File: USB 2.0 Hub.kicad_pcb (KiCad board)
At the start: 2 copper layers, 57.4 x 27.9 mm, 32 parts, among them J1 USB_C_Receptacle_USB2.0, J2 USB_C_Receptacle_USB2.0, J3 USB_C_Receptacle_USB2.0, J4 USB_C_Receptacle_USB2.0, J5 USB_C_Receptacle_USB2.0, U1 SL2.1A

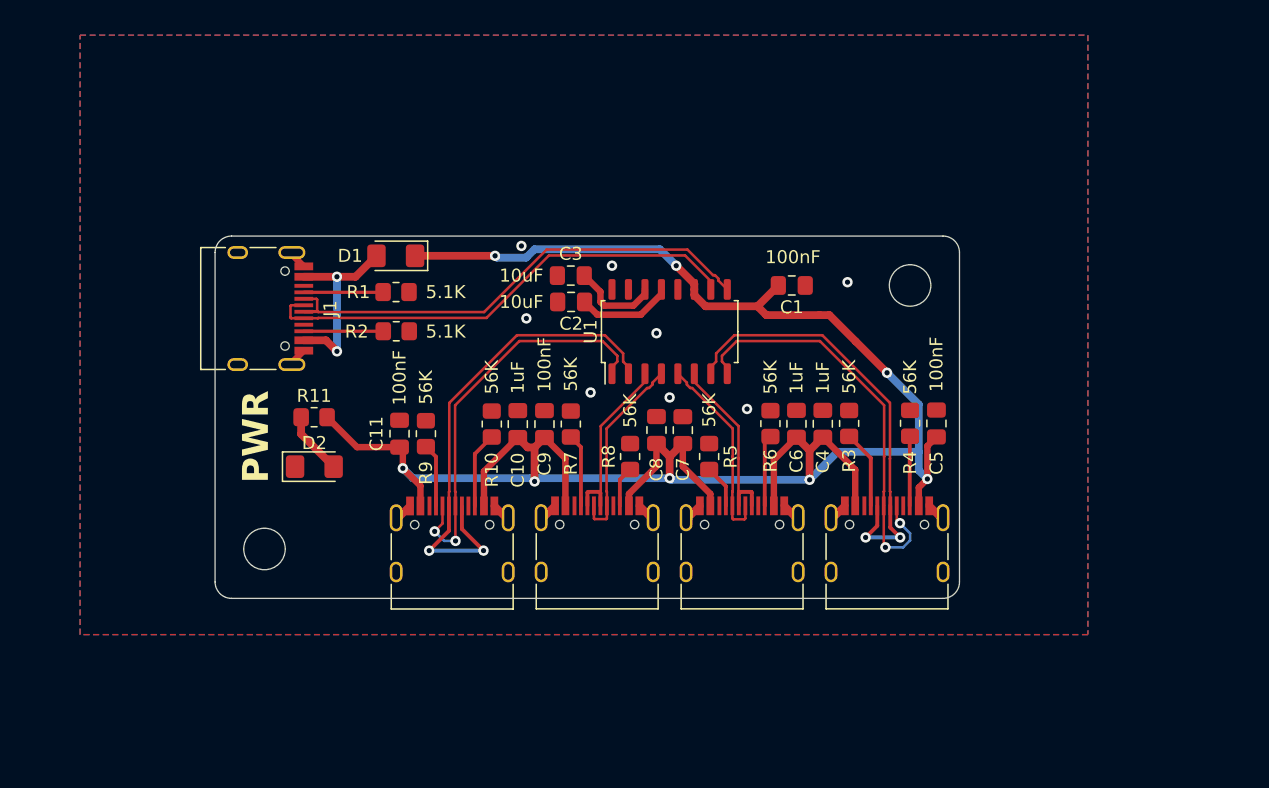
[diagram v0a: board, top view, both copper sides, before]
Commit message: Adjusting size to match wellplate
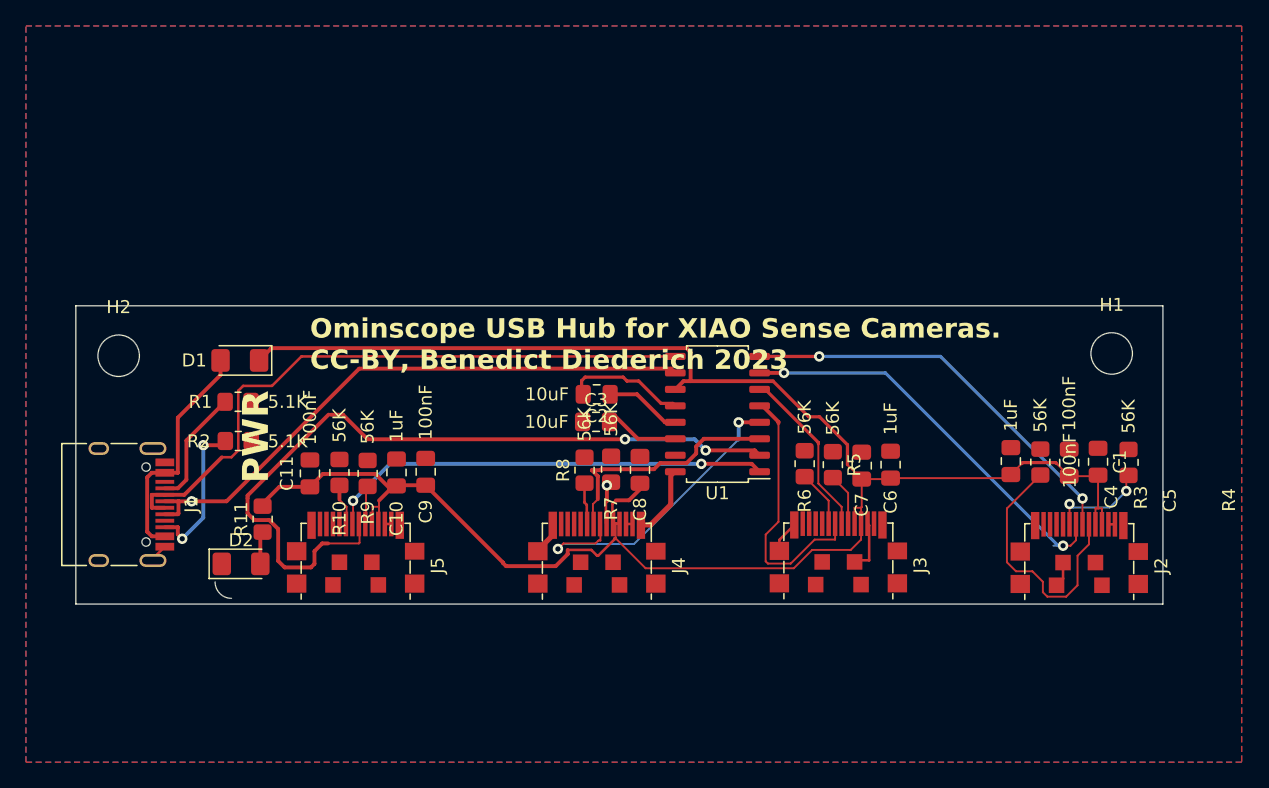
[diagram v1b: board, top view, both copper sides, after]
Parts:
- removed REF** (x2): MountingHole_3.2mm_M3, MountingHole:MountingHole_3.2mm_M3
- added H1: MountingHole, MountingHole:MountingHole_3.2mm_M3_ISO14580, F.Cu at (122.2, 89.8)
- added H2: MountingHole, MountingHole:MountingHole_3.2mm_M3_ISO14580, F.Cu at (45.6, 90.0)
- J2, J3, J4, J5: footprint Connector_USB:USB_C_Receptacle_HRO_TYPE-C-31-M-12 -> uc32_standalone_singlemotor:USB_C_Plug_UTC009-C12
- moved C1 27.2 mm to (121.2, 98.2), turned to -90 degrees
- moved J1 18.5 mm to (45.2, 101.5)
- moved R4 17.1 mm to (123.5, 98.2)
- moved R3 15.0 mm to (116.7, 98.2)
- moved J2 15.0 mm to (119.7, 103.2)
- moved R1 14.8 mm to (54.9, 93.6)
- moved R2 14.8 mm to (54.9, 96.6)
- moved C4 14.8 mm to (114.5, 98.1)
- moved D1 14.5 mm to (55.0, 90.4)
- moved C7 14.1 mm to (103.0, 98.5)
- moved R10 12.3 mm to (62.7, 99.0)
- moved C3 11.4 mm to (82.5, 95.1)
- moved C5 10.7 mm to (119.0, 98.2)
- moved C10 10.1 mm to (67.1, 99.0)
- moved C9 9.87 mm to (69.3, 99.0)
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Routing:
- net /D4+: track 38.2 -> 59.4 mm
- net GND: track 14.5 -> 28.9 mm, vias 8 -> 0
- net Net-(J2-CC1): track 6.05 -> 20.2 mm
- net /VBUS: track 162.8 -> 150.6 mm, vias 8 -> 0
- net /D-: track 39.0 -> 49.5 mm
- net /D3+: track 15.0 -> 25.2 mm, vias 0 -> 2
- net /D+: track 37.8 -> 45.8 mm, vias 0 -> 1
- net Net-(J1-CC2): track 6.13 -> 11.8 mm, vias 0 -> 2
- net /D2-: track 15.0 -> 20.6 mm
- net /D3-: track 14.7 -> 18.7 mm
- net /D4-: track 31.2 -> 34.5 mm
- net Net-(D1-A): track 14.9 -> 18.2 mm, vias 2 -> 0
- net Net-(J1-CC1): track 6.12 -> 9.19 mm
- net Net-(J5-CC2): track 5.86 -> 3.10 mm
- net Net-(J2-CC2): track 5.38 -> 7.86 mm, vias 0 -> 2
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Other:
- board size 57.4 x 27.9 mm -> 83.8 x 23 mm
- board text added: "Ominscope USB Hub for XIAO Sense Cameras. CC-BY, Benedict Diederich 2023"

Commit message: Fixed pending connections
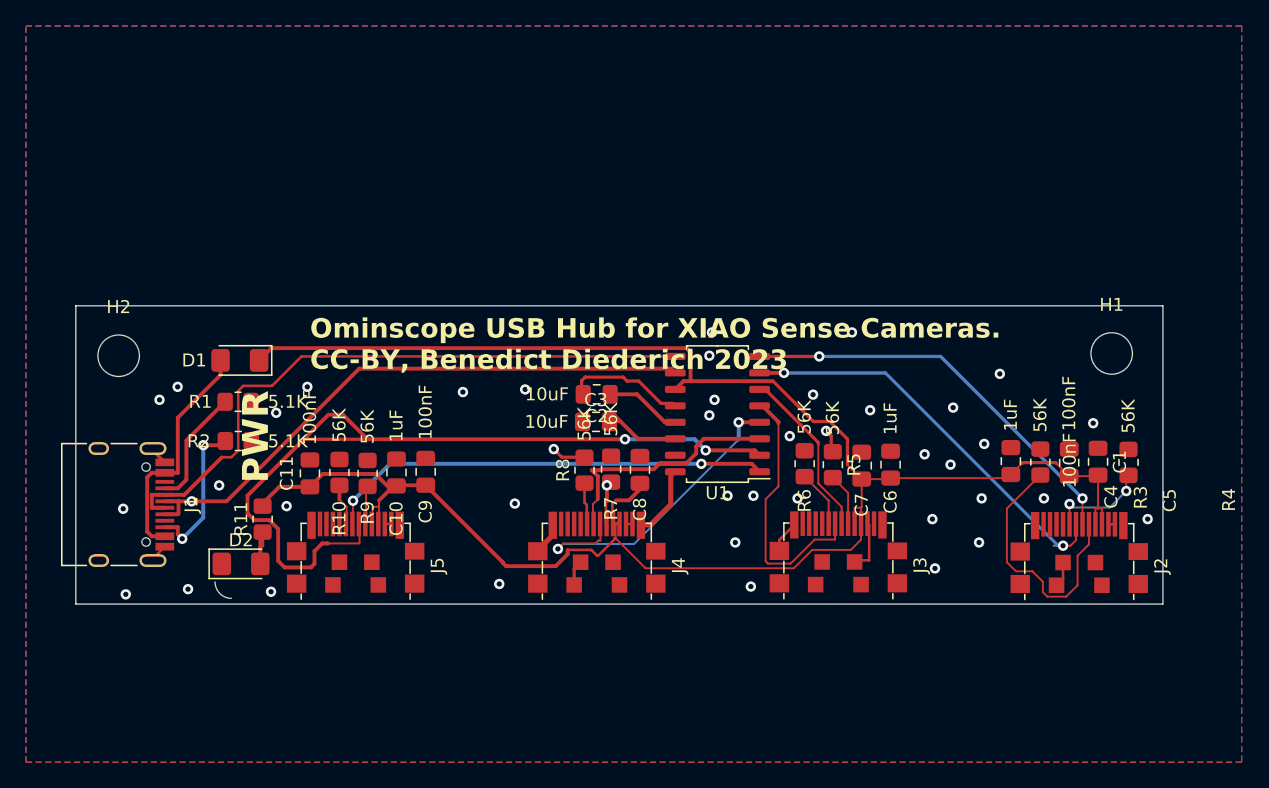
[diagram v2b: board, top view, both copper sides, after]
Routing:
- net GND: track 28.9 -> 36.9 mm, vias 0 -> 41
- net /D4+: track 59.4 -> 64.2 mm
- net Net-(D2-A): track 2.47 -> 3.76 mm
- net Net-(U1-VDD18): track 5.84 -> 6.70 mm

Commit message: Swapping USB connectors
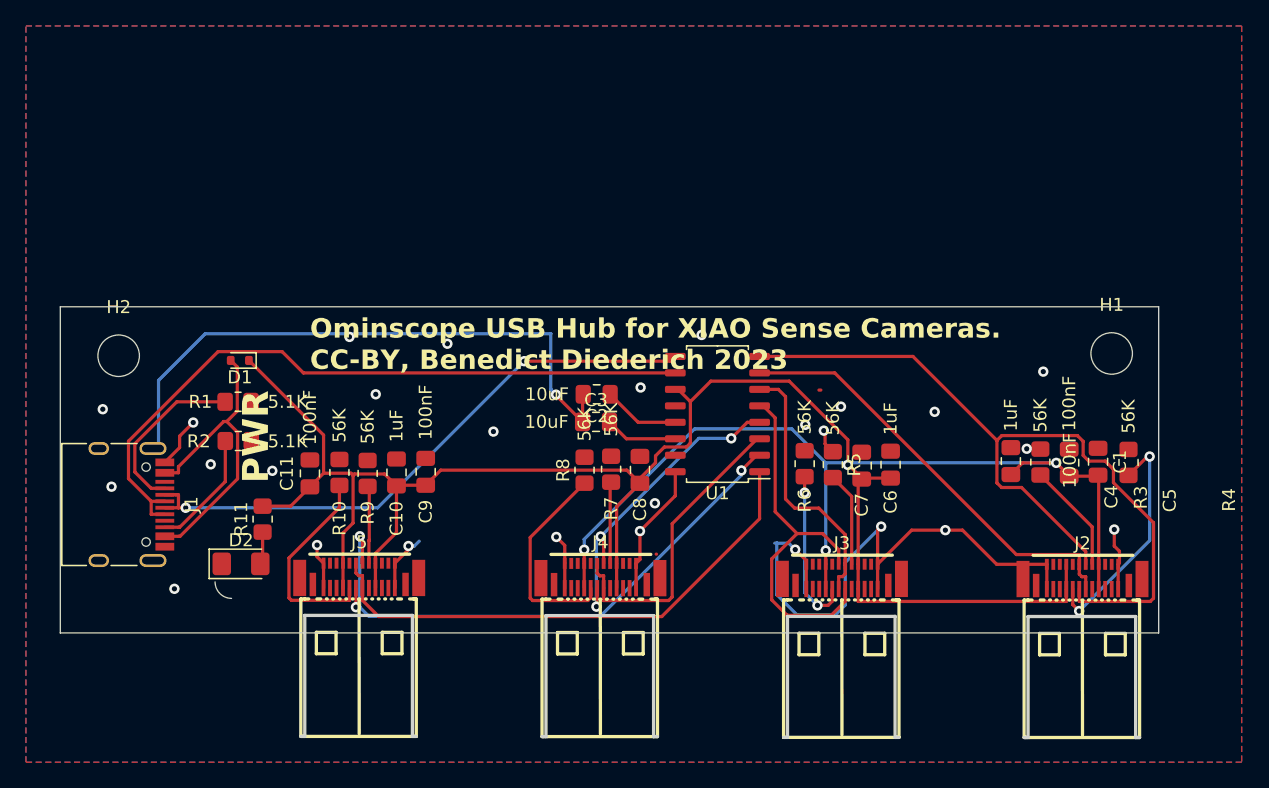
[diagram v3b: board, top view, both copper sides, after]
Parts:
- D1: value SD1206T020S1R0 -> RB521S30T1G; footprint Diode_SMD:D_1206_3216Metric_Pad1.42x1.75mm_HandSolder -> Diode_SMD:D_SOD-523
- J2, J3, J4, J5: footprint uc32_standalone_singlemotor:USB_C_Plug_UTC009-C12 -> Connector_USB:USB_C_Receptacle_U261-241N-4BS2SS
- moved J3 6.96 mm to (101.4, 110.1)
- moved J2 6.91 mm to (120.0, 110.1)
- moved J4 6.87 mm to (82.8, 110.0)
- moved J5 6.86 mm to (64.2, 110.0)
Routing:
- net GND: track 36.9 -> 125.1 mm, vias 41 -> 28
- net /VBUS: track 151.0 -> 199.2 mm, vias 0 -> 4
- net /D1+: track 31.4 -> 63.1 mm, vias 2 -> 0
- net /D4+: track 64.2 -> 45.9 mm, vias 2 -> 3
- net Net-(J4-CC2): track 3.20 -> 16.2 mm
- net Net-(J5-CC2): track 3.10 -> 16.0 mm
- net Net-(J2-CC1): track 20.2 -> 8.54 mm
- net Net-(J2-CC2): track 7.86 -> 18.3 mm
- net /D2-: track 20.6 -> 29.5 mm
- net /D+: track 45.8 -> 54.2 mm, vias 1 -> 0
- net Net-(J3-CC2): track 4.39 -> 12.6 mm, vias 0 -> 2
- net /D2+: track 13.2 -> 20.4 mm
- net /D4-: track 34.5 -> 41.1 mm, vias 2 -> 0
- net Net-(D1-A): track 18.2 -> 24.2 mm
- net /D3-: track 18.7 -> 23.7 mm
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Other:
- board size 83.8 x 23 mm -> 84.7 x 25.2 mm

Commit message: updating outline
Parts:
- moved D1 4.25 mm to (55.5, 94.6)
- moved R1 2.77 mm to (54.8, 96.3)
- moved R2 2.00 mm to (54.9, 98.6)
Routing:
- net /D1+: track 63.1 -> 37.3 mm
- net /VBUS: track 199.2 -> 189.0 mm, vias 4 -> 7
- net /D2-: track 29.5 -> 20.6 mm, vias 0 -> 2
- net Net-(J5-CC2): track 16.0 -> 8.23 mm, vias 0 -> 2
- net /D3-: track 23.7 -> 29.3 mm, vias 0 -> 4
- net Net-(D1-A): track 24.2 -> 18.9 mm
- net GND: track 125.1 -> 130.1 mm
- net Net-(J4-CC2): track 16.2 -> 11.7 mm, vias 0 -> 2
- net /D1-: track 33.5 -> 37.8 mm, vias 0 -> 2
- net Net-(J2-CC2): track 18.3 -> 14.5 mm, vias 2 -> 3
- net /D4+: track 45.9 -> 42.6 mm, vias 3 -> 2
- net /D3+: track 25.1 -> 22.0 mm, vias 3 -> 4
- net Net-(J3-CC2): track 12.6 -> 9.72 mm
- net Net-(J1-CC2): track 9.25 -> 7.26 mm
- net /D+: track 54.2 -> 52.8 mm
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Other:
- board size 84.7 x 25.2 mm -> 83.7 x 22.5 mm
